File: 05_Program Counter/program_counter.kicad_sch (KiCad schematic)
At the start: 38 parts, among them U1 74LS161, U2 74LS245, U3 74LS161, U4 74LS161, U5 74LS245, U6 74LS161

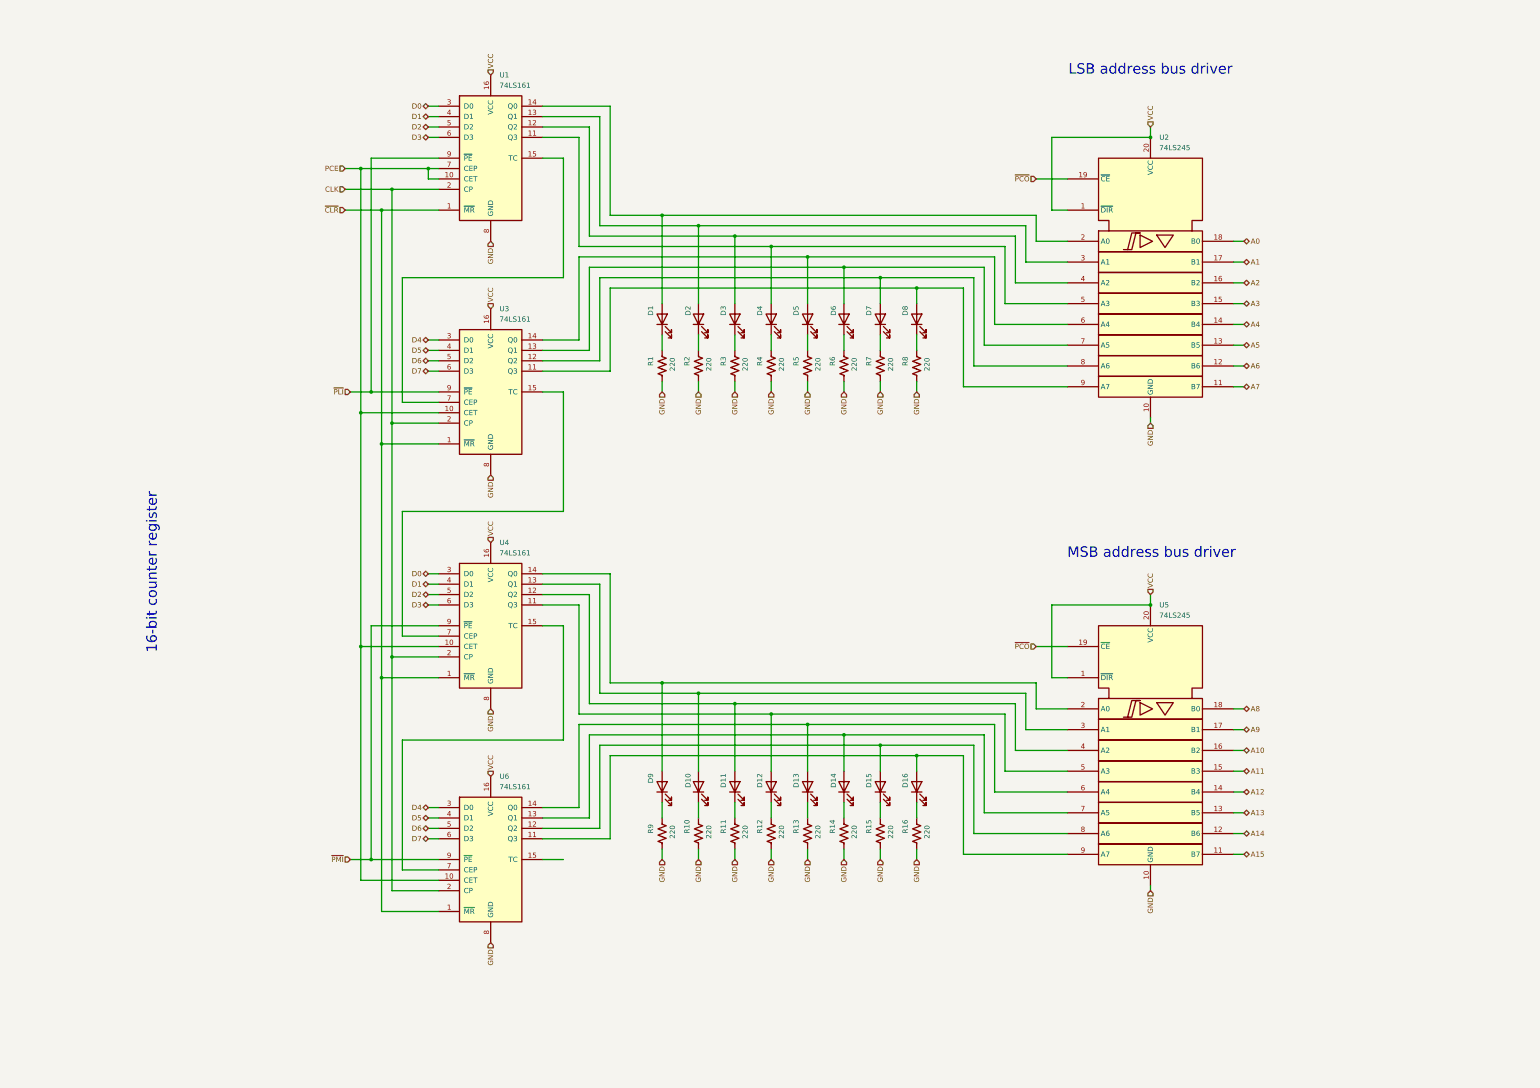
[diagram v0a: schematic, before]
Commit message: Last revision of the cpu, all boards have been ordered. Implementation to be tested and documented in following commits.
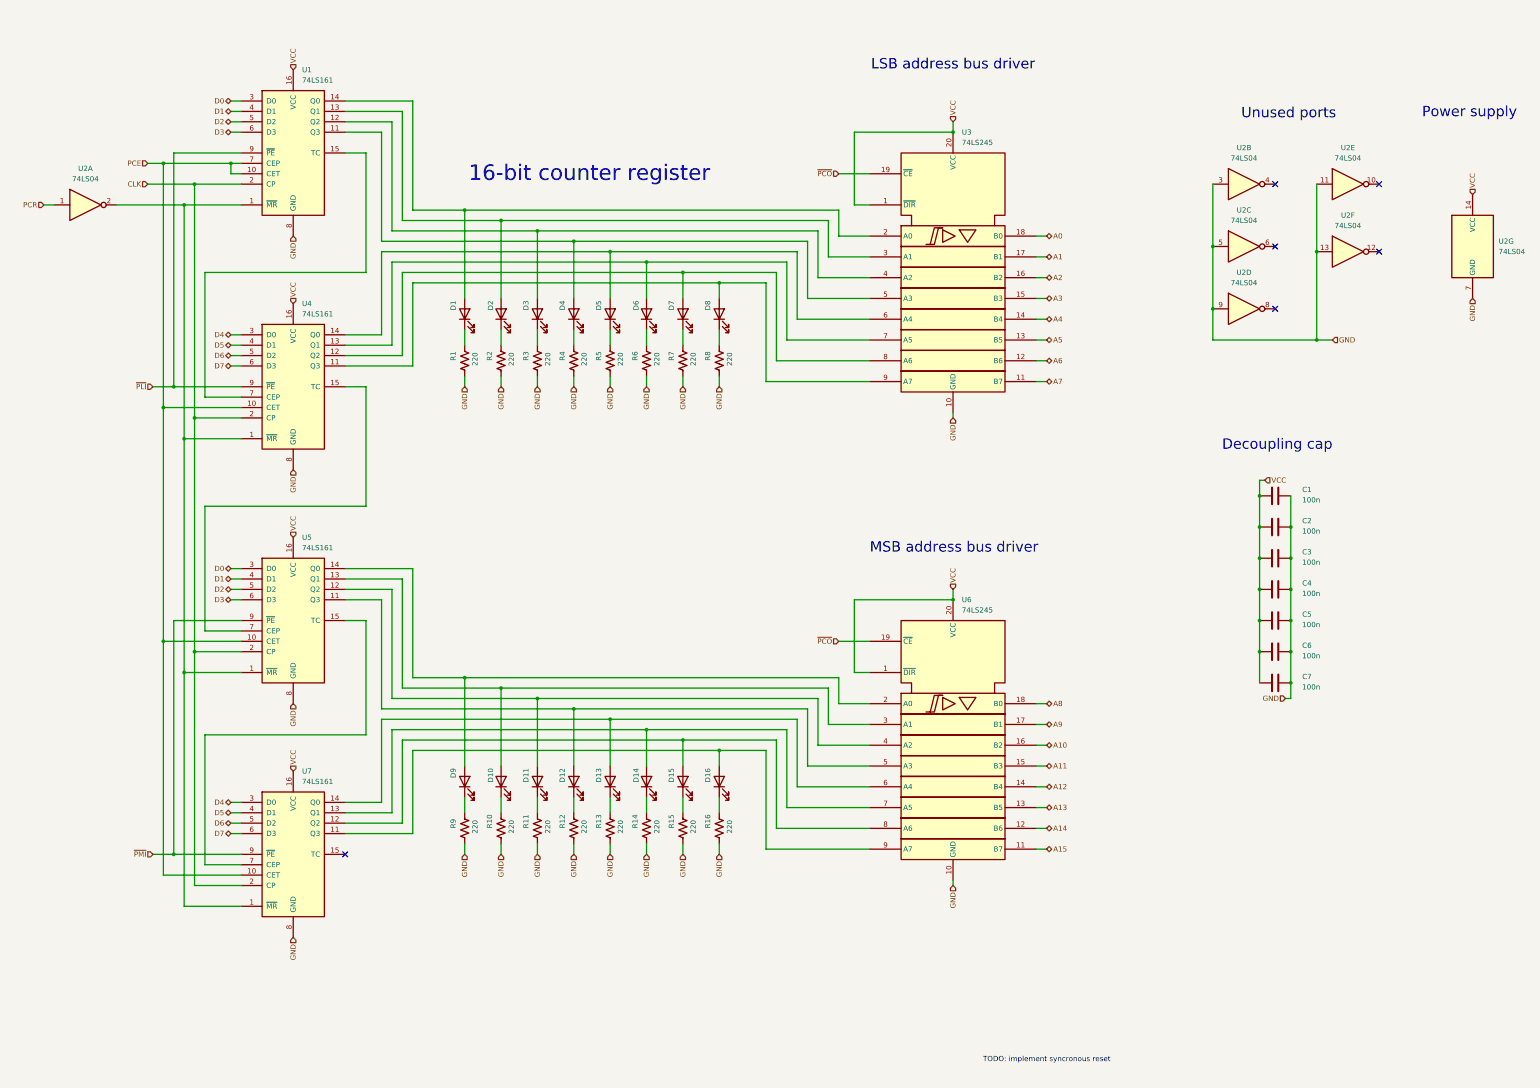
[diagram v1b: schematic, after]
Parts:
- added C1, C2, C3, C4, C5, C6, C7: 100n, Capacitor_THT:C_Disc_D3.0mm_W1.6mm_P2.50mm, symbol Device:C
- added U2: 74LS04, Package_DIP:DIP-14_W7.62mm, symbol 74xx:74LS04
- renumbered U2 to U3, U3 to U4, U4 to U5, U5 to U6, U6 to U7
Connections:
- net GND: now also C1.2, C2.2, C3.2, C4.2, C5.2, C6.2, C7.2, U2.11, U2.13, U2.3, U2.5, U2.7 (GND), U2.9
- net VCC: now also C1.1, C2.1, C3.1, C4.1, C5.1, C6.1, C7.1, U2.14 (VCC)
- net ~{CLR}: no longer names the net of U1.1 (~{MR}), U4.1 (~{MR}), U5.1 (~{MR}), U7.1 (~{MR})
- net ~{CLR}: now also U2.2
- new net PCR: U2.1
- no-connect marks 0 -> 6
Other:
- note added: "Decoupling cap"
- note added: "Power supply"
- note added: "Unused ports"
- moved on the sheet: D1, D10, D11, D12, D13, D14, D15, D16, D2, D3, D4, D5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

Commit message: Update 10-01-2026 - Fixed bug on program counter - Fist ISA review, still in draft - Added missing mounting holes on memory modules
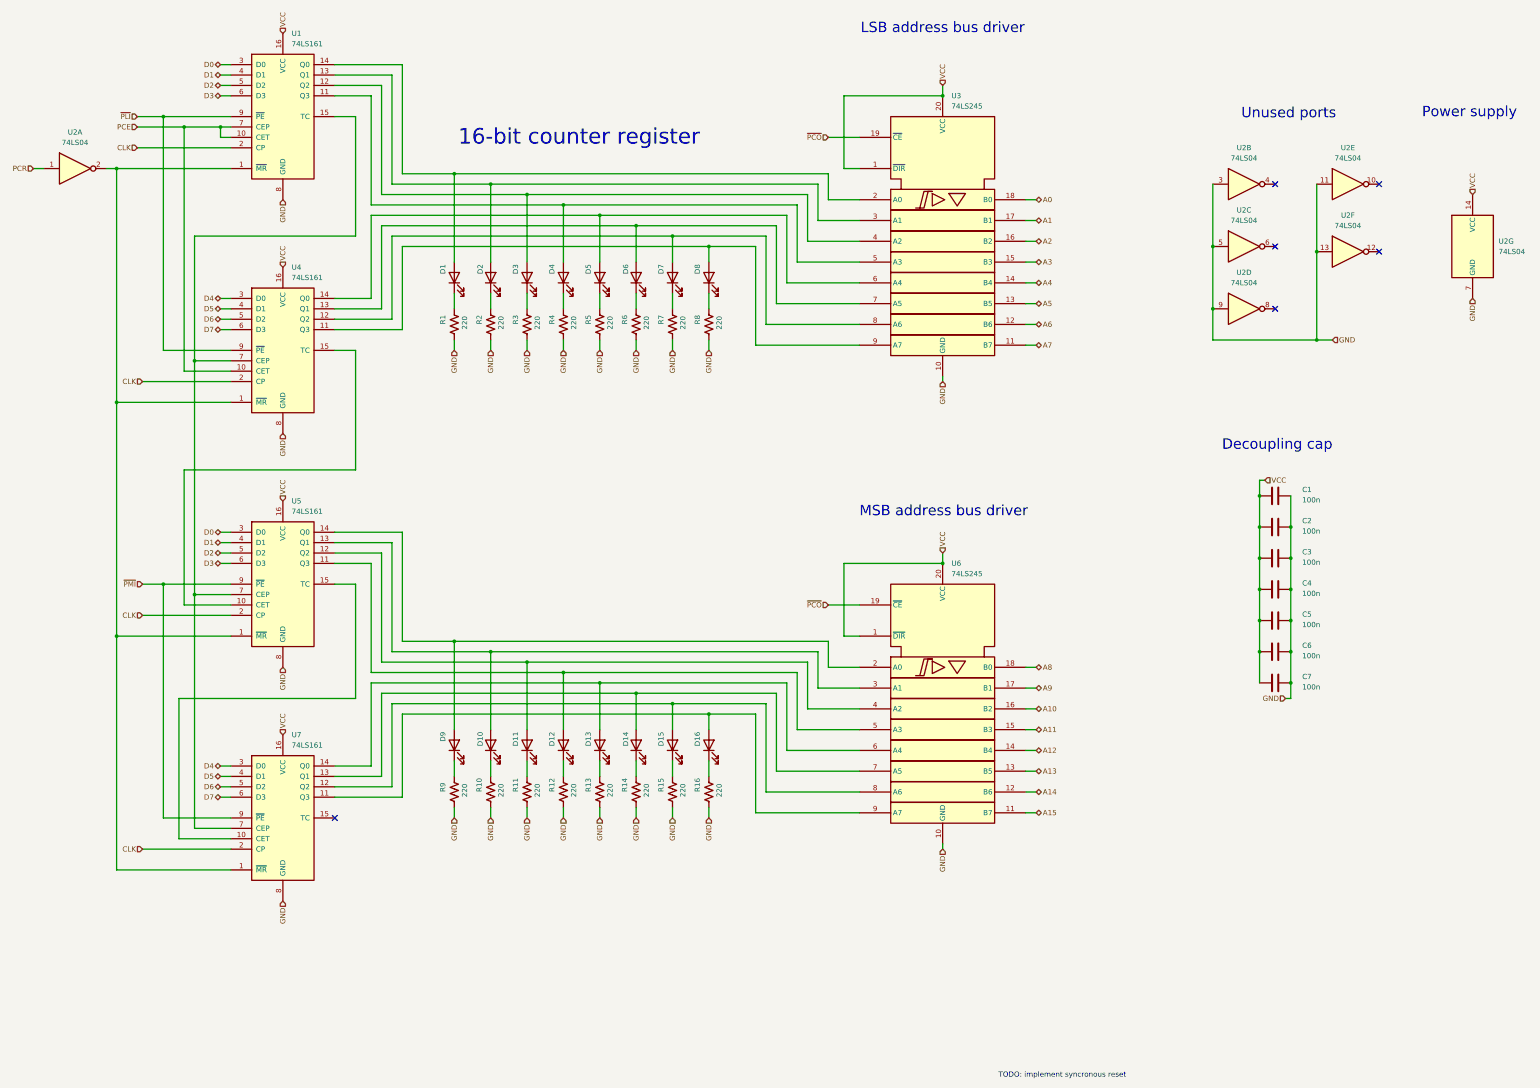
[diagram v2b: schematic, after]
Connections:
- net PCE: no longer U5.10 (CET), U7.10 (CET)
- net at U4.15 (TC): now also U5.10 (CET); no longer U5.7 (CEP)
- net at U1.15 (TC), U4.7 (CEP): now also U5.7 (CEP), U7.7 (CEP)
- net at U5.15 (TC): now also U7.10 (CET); no longer U7.7 (CEP)
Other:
- moved on the sheet: D1, D10, D11, D12, D13, D14, D15, D16, D2, D3, D4, D5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
